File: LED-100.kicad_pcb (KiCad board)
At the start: 2 copper layers, 100 x 100 mm, 101 parts, among them J2 LDA100_2_J2, J3 LDA100_2_J3, J4 LDA100_2_J4, J5 xtra, J7 Conn_01x01, J8 Conn_01x06, SW1 SW_SPDT, U1 TLC5947DAP, U2 TLC5947DAP, U3 TLC5947DAP, U4 TEENSY 4.0

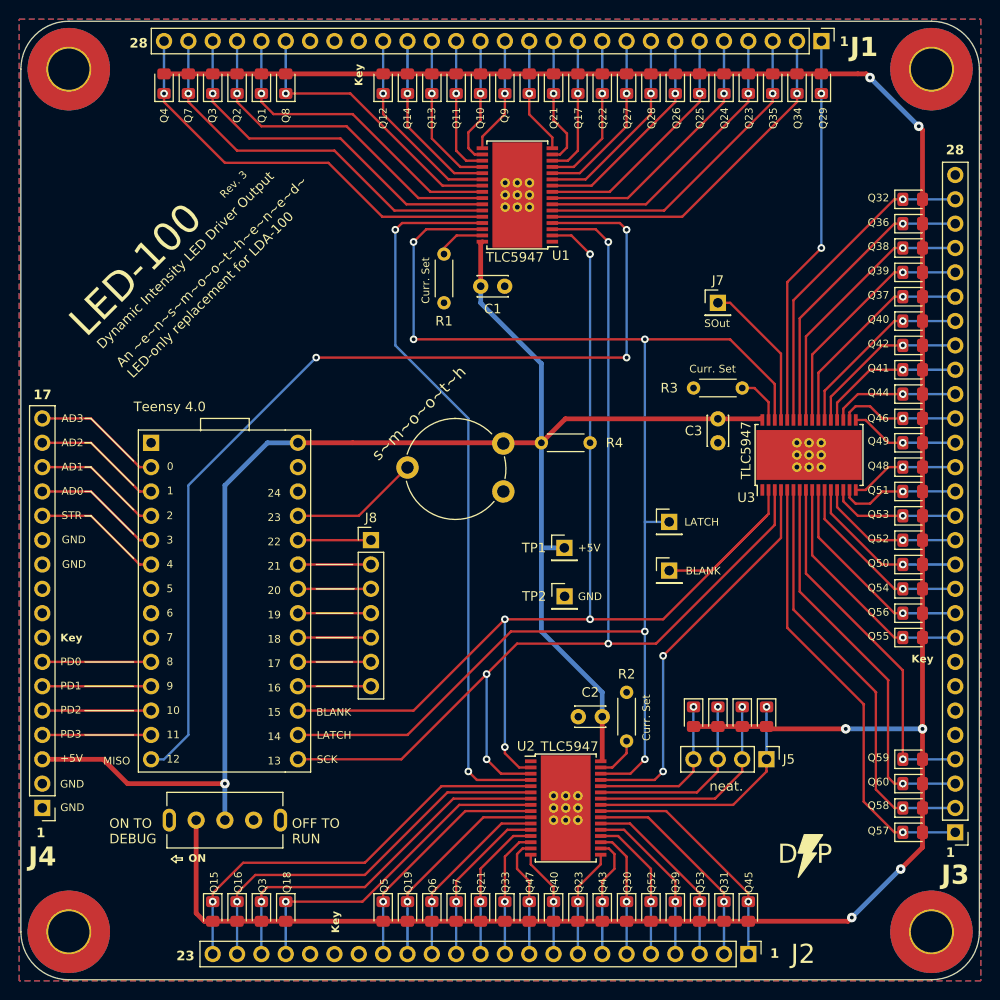
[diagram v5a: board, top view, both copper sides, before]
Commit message: Angled teensy + updates (#1)
* diagonal teensy, pin reassignments, tweaks

* added a switch, updated to kicad 9

* rev3
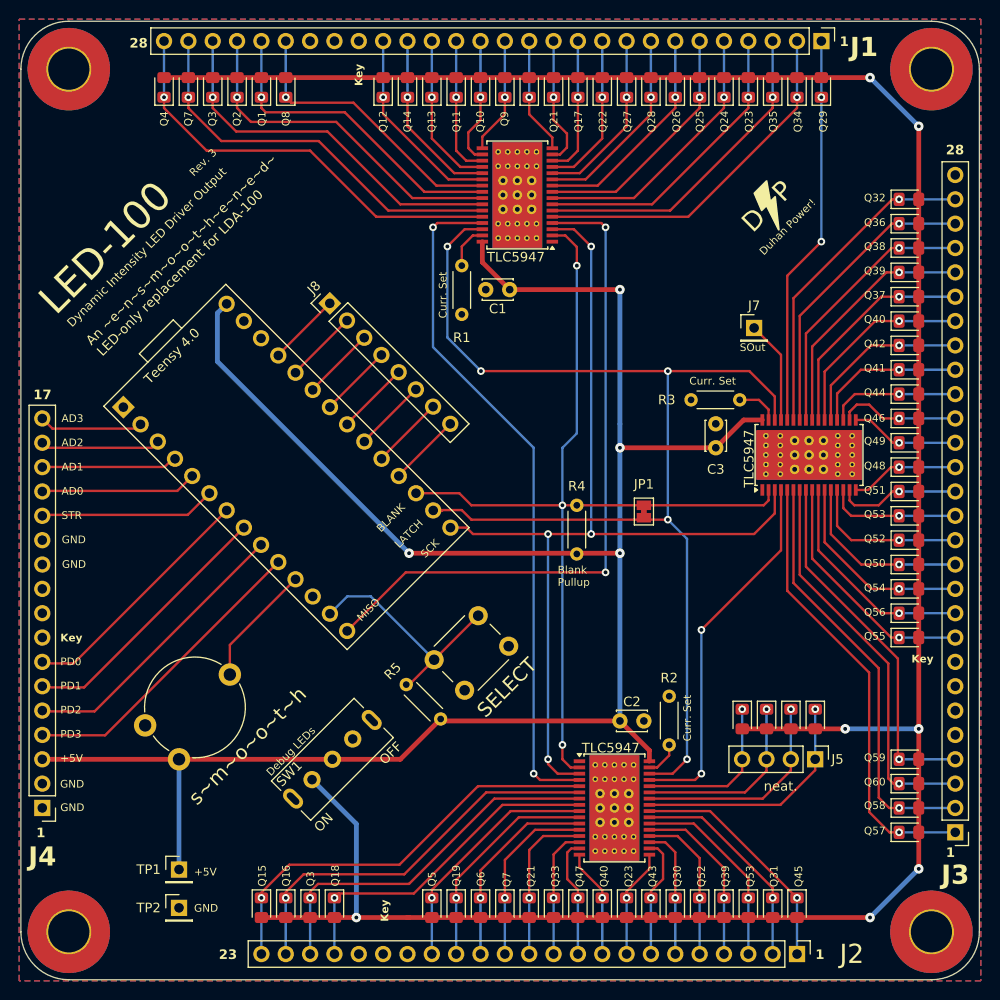
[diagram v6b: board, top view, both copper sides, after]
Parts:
- removed BLANK, LATCH: Conn_01x01, Connector_PinHeader_2.54mm:PinHeader_1x01_P2.54mm_Vertical
- added JP1: SolderJumper_2_Bridged, Jumper:SolderJumper-2_P1.3mm_Bridged_Pad1.0x1.5mm, F.Cu at (165.0, 101.2)
- added R5: 100k, Resistor_THT:R_Axial_DIN0204_L3.6mm_D1.6mm_P5.08mm_Horizontal, F.Cu at (143.8, 122.8)
- added SELECT: SW_SPST, Button_Switch_THT:SW_PUSH_6mm_H5mm, F.Cu at (150.9, 115.2)
- J8: value Conn_01x06 -> Conn_01x08; footprint Connector_PinHeader_2.54mm:PinHeader_1x07_P2.54mm_Vertical -> Connector_PinHeader_2.54mm:PinHeader_1x08_P2.54mm_Vertical
- SW1: footprint Button_Switch_THT:SW_Slide_SPDT_SLW-12689-4A-N-D -> MyParts:SWITCH_SPDT-SLW-12689-4A-N-D
- U1, U2, U3: footprint Package_SO:HTSSOP-32-1EP_6.1x11mm_P0.65mm_EP5.2x11mm_Mask4.11x4.36mm_ThermalVias -> MyParts:Package_SO_HTSSOP-32-1EP_6.1x11mm_P0.65mm_EP5.2x11mm_Mask4.11x4.36mm_ThermalVias
- U4: footprint Connector_PinHeader_2.54mm:PinHeader_2x1x14_P2.54mm_Vertical -> MyParts:Teensy 4.0
- moved REF** 74.8 mm to (107.5, 135.0), turned to 90 degrees
- moved TP1 52.4 mm to (116.5, 138.5)
- moved TP2 51.7 mm to (116.5, 142.5)
- moved RV1 47.2 mm to (116.5, 127.0), turned to 45 degrees
- moved J8 25.1 mm to (132.2, 79.4), turned to 45 degrees
- moved U4 14.7 mm to (126.9, 95.6), turned to 45 degrees
- moved SW1 12.9 mm to (132.5, 127.0), turned to 45 degrees
- moved R4 12.2 mm to (158.0, 105.6), turned to 90 degrees
- moved D30 5.09 mm to (168.3, 142.5)
- moved D31 5.09 mm to (178.4, 142.5)
- moved D3b1 5.09 mm to (130.2, 142.5)
- moved D40b1 5.09 mm to (160.7, 142.5)
- moved D43 5.09 mm to (165.7, 142.5)
- moved D47 5.09 mm to (158.1, 142.5)
- moved D5 5.09 mm to (142.9, 142.5)
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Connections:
- net /BLANK renamed BLANK
- net /LAT renamed LAT
- net /MISO_A renamed MISO_A
- net /MISO_B renamed MISO_B
- net /MISO_C renamed MISO_C
- net /Q1 renamed Q1
- net /Q10 renamed Q10
- net /Q11 renamed Q11
- net /Q12 renamed Q12
- net /Q13 renamed Q13
- net /Q14 renamed Q14
- net /Q15 renamed Q15
- net /Q16 renamed Q16
- net /Q17 renamed Q17
- net /Q18 renamed Q18
- net /Q19 renamed Q19
- net /Q2 renamed Q2
- net /Q20 renamed Q20
- net /Q21a renamed Q21a
- net /Q21b renamed Q21b
- net /Q22 renamed Q22
- net /Q23a renamed Q23a
- net /Q23b renamed Q23b
- net /Q24 renamed Q24
- net /Q25 renamed Q25
- net /Q26 renamed Q26
- net /Q27 renamed Q27
- net /Q28 renamed Q28
- net /Q29 renamed Q29
- net /Q30 renamed Q30
- net /Q31 renamed Q31
- net /Q32 renamed Q32
- net /Q33 renamed Q33
- net /Q34 renamed Q34
- net /Q35 renamed Q35
- net /Q36 renamed Q36
- net /Q37 renamed Q37
- net /Q38 renamed Q38
- net /Q39a renamed Q39a
- net /Q39b renamed Q39b
- net /Q3a renamed Q3a
- net /Q3b renamed Q3b
- net /Q4 renamed Q4
- net /Q40a renamed Q40a
- net /Q40b renamed Q40b
- net /Q41 renamed Q41
- net /Q42 renamed Q42
- net /Q43 renamed Q43
- net /Q44 renamed Q44
- net /Q45 renamed Q45
- net /Q46 renamed Q46
- net /Q47 renamed Q47
- net /Q48 renamed Q48
- net /Q49 renamed Q49
- net /Q5 renamed Q5
- net /Q50 renamed Q50
- net /Q51 renamed Q51
- net /Q52a renamed Q52a
- net /Q52b renamed Q52b
- net /Q53a renamed Q53a
- net /Q53b renamed Q53b
- net /Q54 renamed Q54
- net /Q55 renamed Q55
- net /Q56 renamed Q56
- net /Q57 renamed Q57
- net /Q58 renamed Q58
- net /Q59 renamed Q59
- net /Q6 renamed Q6
- net /Q60 renamed Q60
- net /Q7a renamed Q7a
- net /Q7b renamed Q7b
- net /Q8 renamed Q8
- net /Q9 renamed Q9
- net /SCK renamed SCK
- net /XTRA1 renamed QX1
- net /XTRA2 renamed QX2
- net /XTRA3 renamed QX3
- net /XTRA4 renamed QX4
- RV1 pad 2: /FADESPEED -> FADESPEED
- U4 pad 10: Net-(J4-PD0) -> Net-(J4-PD3)
- U4 pad 11: Net-(J4-PD1) -> FADESPEED
- U4 pad 12: Net-(J4-PD2) -> unconnected-(U4-10-Pad12)
- U4 pad 13: Net-(J4-PD3) -> SW_SELECT
- U4 pad 18: Net-(J8-Pin_7) -> Net-(J8-Pin_8)
- U4 pad 19: Net-(J8-Pin_6) -> Net-(J8-Pin_7)
- U4 pad 20: Net-(J8-Pin_5) -> Net-(J8-Pin_6)
- U4 pad 21: Net-(J8-Pin_4) -> Net-(J8-Pin_5)
- U4 pad 22: Net-(J8-Pin_3) -> Net-(J8-Pin_4)
- U4 pad 23: Net-(J8-Pin_2) -> Net-(J8-Pin_3)
- U4 pad 24: Net-(J8-Pin_1) -> Net-(J8-Pin_2)
- U4 pad 25: /FADESPEED -> Net-(J8-Pin_1)
- U4 pad 7: unconnected-(U4-5-Pad7) -> Net-(J4-PD0)
- U4 pad 8: unconnected-(U4-6-Pad8) -> Net-(J4-PD1)
- U4 pad 9: unconnected-(U4-7-Pad9) -> Net-(J4-PD2)
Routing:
- net +5V: track 175.7 -> 214.2 mm, vias 1 -> 4
- net BLANK: track 133.3 -> 97.9 mm, vias 4 -> 3
- net MISO_A: track 103.6 -> 71.1 mm, vias 3 -> 2
- net LAT: track 154.1 -> 123.8 mm
- net SCK: track 126.5 -> 99.9 mm
- net SW_SELECT: track 0.00 -> 24.8 mm
- net Net-(J4-PD3): track 11.4 -> 32.3 mm
- net Net-(J4-PD2): track 11.4 -> 30.4 mm
- net Net-(J4-PD1): track 11.4 -> 28.2 mm
- net Net-(J4-PD0): track 11.4 -> 26.1 mm
- net /FADESPEED: track 13.5 -> 0.00 mm
- net FADESPEED: track 0.00 -> 12.8 mm
- net Net-(J8-Pin_8): track 0.00 -> 7.60 mm
- net /TEST5V: track 269.4 -> 263.5 mm, vias 6 -> 7
- net Net-(J4-Strobe): track 13.5 -> 18.7 mm
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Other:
- board text added: "Blank Pullup"
- board text added: "Debug LEDs"
- board text added: "OFF"
- board text added: "Schematics, source, and code: https://github.com/andrewduhan/LED-100"
- board text removed: "0"
- board text removed: "10"
- board text removed: "11"
- board text removed: "12"
- board text removed: "13"
- board text removed: "14"
- board text removed: "15"
- board text removed: "16"
- board text removed: "18"
- board text removed: "19"
- board text removed: "2"
- board text removed: "20"
- board text removed: "21"
- board text removed: "22"
- board text removed: "24"
- board text removed: "3"
- board text removed: "4"
- board text removed: "5"
- board text removed: "6"
- board text removed: "7"
- board text removed: "8"
- board text removed: "9"
- board text removed: "OFF TO RUN"
- board text removed: "ON TO DEBUG"
- board text removed: "Schematics, source, and code:"
- board text removed: "https://github.com/andrewduhan/LED-100"

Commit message: trying a wider version, WIP
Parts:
- removed D21a1, D21b1, D23a1, D23b1, D39a1, D39b1, D3a1, D3b1, D40a1, D40b1, D52a1, D52b1, D53a1, D53b1, D7a1, D7b1: LED_Small, LED_SMD:LED_0805_2012Metric_Pad1.15x1.40mm_HandSolder
- removed SELECT: SW_SPST, Button_Switch_THT:SW_PUSH_6mm_H5mm
- added D21: LED_Small, LED_THT:LED_D3.0mm, F.Cu at (188.0, 73.5)
- added D23: LED_Small, LED_THT:LED_D3.0mm, F.Cu at (170.0, 79.5)
- added D3: LED_Small, LED_THT:LED_D3.0mm, F.Cu at (212.0, 67.5)
- added D39: LED_Small, LED_THT:LED_D3.0mm, F.Cu at (180.0, 100.5)
- added D40: LED_Small, LED_THT:LED_D3.0mm, F.Cu at (174.0, 106.5)
- added D52: LED_Small, LED_THT:LED_D3.0mm, F.Cu at (156.0, 106.5)
- added D53: LED_Small, LED_THT:LED_D3.0mm, F.Cu at (162.0, 94.5)
- added D61: LED_Small, LED_THT:LED_D3.0mm, F.Cu at (90.0, 90.5)
- added D62: LED_Small, LED_THT:LED_D3.0mm, F.Cu at (102.0, 84.5)
- added D63: LED_Small, LED_THT:LED_D3.0mm, F.Cu at (102.0, 90.5)
- added D64: LED_Small, LED_THT:LED_D3.0mm, F.Cu at (108.0, 90.5)
- added D65: LED_Small, LED_THT:LED_D3.0mm, F.Cu at (114.0, 78.5)
- added D66: LED_Small, LED_THT:LED_D3.0mm, F.Cu at (120.0, 78.5)
- added D67: LED_Small, LED_THT:LED_D3.0mm, F.Cu at (120.0, 84.5)
- added D68: LED_Small, LED_THT:LED_D3.0mm, F.Cu at (120.0, 90.5)
- added D7: LED_Small, LED_THT:LED_D3.0mm, F.Cu at (212.0, 73.5)
- added SW2: SW_SPST, Button_Switch_THT:SW_PUSH_6mm_H5mm, F.Cu at (54.0, 146.0)
- D1, D10, D11, D12, D13, D14, D15, D16, D17, D18, D19, D2, D20, D22, D24, D25, D26, D27, D28, D29, D30, D31, D32, D33, D34, D35, D36, D37, D38, D4, D41, D42, D43, D44, D45, D46, D47, D48, D49, D5, D50, D51, D54, D55, D56, D57, D58, D59, D6, D60, D69, D70, D71, D72, D8, D9: footprint LED_SMD:LED_0805_2012Metric_Pad1.15x1.40mm_HandSolder -> LED_THT:LED_D3.0mm
- J8: value Conn_01x08 -> Conn_01x07; footprint Connector_PinHeader_2.54mm:PinHeader_1x08_P2.54mm_Vertical -> Connector_PinHeader_2.54mm:PinHeader_1x07_P2.54mm_Vertical
- moved H2 197.4 mm to (22.0, 150.0)
- moved H3 174.5 mm to (258.0, 61.0)
- moved REF** 139.1 mm to (246.0, 147.5), turned to 180 degrees
- moved J1 115.8 mm to (260.0, 139.0), turned to 180 degrees
- moved U1 104.5 mm to (248.7, 107.3), turned to 90 degrees
- moved D4 99.7 mm to (212.0, 79.5)
- moved R1 99.0 mm to (241.5, 101.5), turned to 90 degrees
- moved JP1 95.7 mm to (73.5, 129.3)
- moved C1 94.2 mm to (241.5, 104.0), turned to -90 degrees
- moved R5 86.9 mm to (58.0, 136.4), turned to -90 degrees
- moved D2 86.5 mm to (206.0, 79.5)
- moved R4 84.2 mm to (76.0, 124.5), turned to 180 degrees
- moved H1 83.2 mm to (22.0, 61.0)
- moved J4 82.8 mm to (20.0, 122.2)
- moved D31 82.7 mm to (126.0, 78.5), turned to 90 degrees
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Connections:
- U1 pad 29: MISO_B -> Net-(J7-Pin_1)
- U1 pad 4: MISO_A -> MISO_C
- U2 pad 29: MISO_C -> MISO_B
- U2 pad 4: MISO_B -> MISO_A
- U3 pad 29: Net-(J7-Pin_1) -> MISO_C
- U3 pad 4: MISO_C -> MISO_B
- U4 pad 11: FADESPEED -> unconnected-(U4-9-Pad11)
- U4 pad 18: Net-(J8-Pin_8) -> Net-(J8-Pin_7)
- U4 pad 19: Net-(J8-Pin_7) -> Net-(J8-Pin_6)
- U4 pad 20: Net-(J8-Pin_6) -> Net-(J8-Pin_5)
- U4 pad 21: Net-(J8-Pin_5) -> Net-(J8-Pin_4)
- U4 pad 22: Net-(J8-Pin_4) -> Net-(J8-Pin_3)
- U4 pad 23: Net-(J8-Pin_3) -> Net-(J8-Pin_2)
- U4 pad 24: Net-(J8-Pin_2) -> Net-(J8-Pin_1)
- U4 pad 25: Net-(J8-Pin_1) -> FADESPEED
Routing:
- net /TEST5V: track 263.5 -> 0.00 mm, vias 7 -> 0
- net BLANK: track 97.9 -> 225.3 mm, vias 3 -> 7
- net SCK: track 99.9 -> 224.1 mm, vias 4 -> 6
- net +5V: track 214.2 -> 335.7 mm, vias 4 -> 7
- net LAT: track 123.8 -> 244.8 mm, vias 5 -> 6
- net Net-(J4-AD3): track 10.7 -> 30.6 mm
- net MISO_B: track 71.7 -> 90.8 mm, vias 2 -> 0
- net MISO_C: track 38.7 -> 57.7 mm
- net Net-(J4-AD2): track 12.5 -> 31.2 mm
- net Net-(J4-AD1): track 14.1 -> 30.6 mm
- net Net-(J4-AD0): track 16.6 -> 31.6 mm
- net QX4: track 16.8 -> 30.7 mm, vias 1 -> 0
- net Net-(J4-Strobe): track 18.7 -> 30.6 mm
- net QX3: track 19.6 -> 31.5 mm, vias 1 -> 0
- net QX2: track 22.4 -> 32.3 mm, vias 1 -> 0
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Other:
- board size 100 x 100 mm -> 246 x 99 mm
- board text added: "Q20"
- board text added: "Rev. 4"
- board text removed: "1"
- board text removed: "Debug LEDs"
- board text removed: "OFF"
- board text removed: "ON"
- board text removed: "Rev. 3"

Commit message: <---wider--->
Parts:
- removed D1, D10, D11, D12, D13, D14, D15, D16, D17, D18, D19, D2, D20, D21, D22, D23, D24, D25, D26, D27, D28, D29, D3, D30, D31, D32, D33, D34, D35, D36, D37, D38, D39, D4, D40, D41, D42, D43, D44, D45, D46, D47, D48, D49, D5, D50, D51, D52, D53, D54, D55, D56, D57, D58, D59, D6, D60, D61, D62, D63, D64, D65, D66, D67, D68, D69, D7, D70, D71, D72, D8, D9: LED_Small, LED_THT:LED_D3.0mm
- removed SW1: SW_SPDT, MyParts:SWITCH_SPDT-SLW-12689-4A-N-D
- moved J5 2.00 mm to (144.0, 147.0)
- moved J8 1.00 mm to (64.0, 107.3)
- moved R4 1.00 mm to (76.0, 123.5)
- moved R5 1.00 mm to (58.0, 135.4)
- moved RV1 1.00 mm to (76.0, 115.0)
- moved SW2 1.00 mm to (54.0, 145.0)
- moved TP1 1.00 mm to (39.5, 135.5)
- moved TP2 1.00 mm to (39.5, 142.5)
- moved U4 1.00 mm to (50.4, 112.2)
- moved C1 0.50 mm to (241.5, 104.5)
- moved J7 0.50 mm to (241.5, 88.0)
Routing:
- net +5V: track 335.7 -> 333.6 mm
- net BLANK: track 225.3 -> 226.8 mm
- net Net-(J4-AD0): track 31.6 -> 30.2 mm
- net Net-(J4-PD0): track 26.3 -> 25.0 mm
- net Net-(J4-AD2): track 31.2 -> 30.2 mm
- net QX4: track 30.7 -> 29.9 mm
- net QX2: track 32.3 -> 31.5 mm
- net QX1: track 33.1 -> 32.2 mm
- net QX3: track 31.5 -> 30.7 mm
